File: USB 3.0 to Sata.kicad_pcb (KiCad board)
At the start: 4 copper layers, 27.8 x 45 mm, 35 parts, among them J1 USB_C_Receptacle, U3 VL716-Q4, U4 XUTS-2205-0429, U5 W25Q16BVSSIG, Y2 25Mhz Crystal

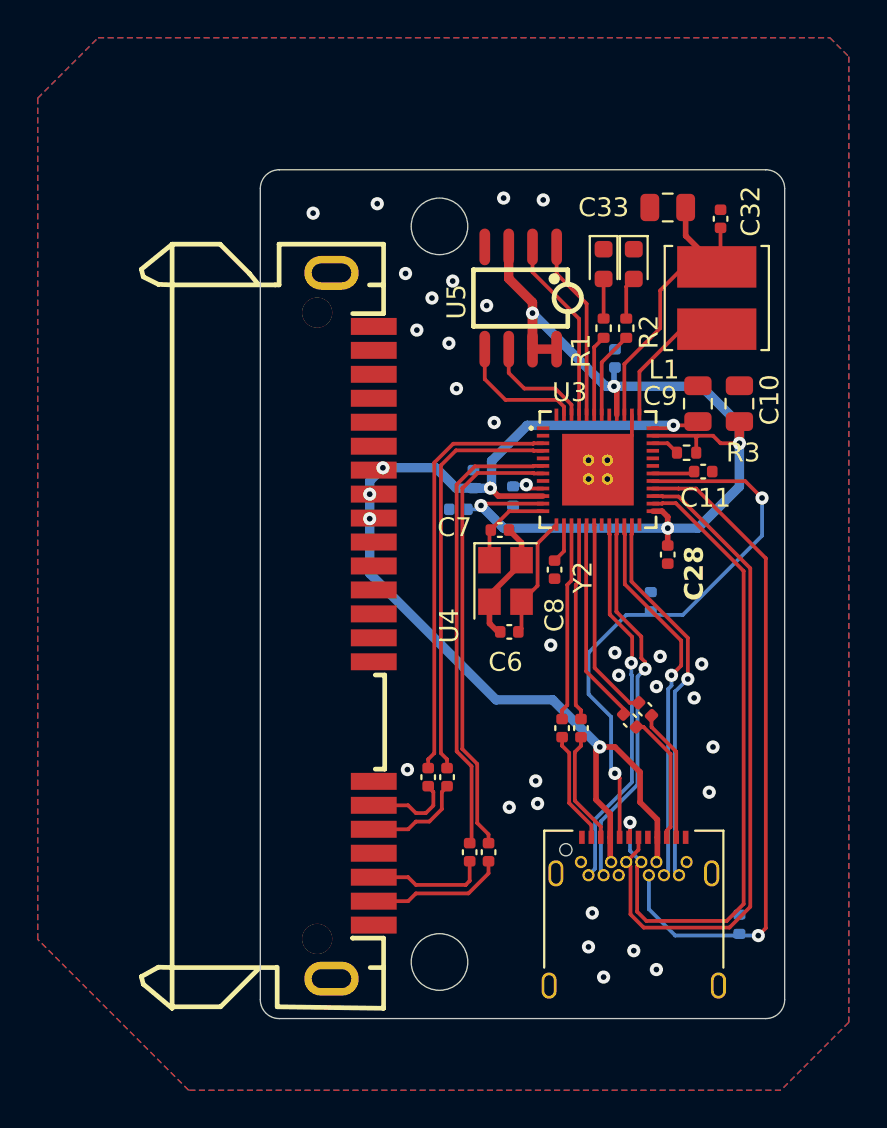
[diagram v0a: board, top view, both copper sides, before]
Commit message: Fixed pcb errors
Fixed RX2 TX2 lines being flipped, changed usb port footprint to the corect one, changed flash footprint from SOP8-150MIL to SOP8-208MIL
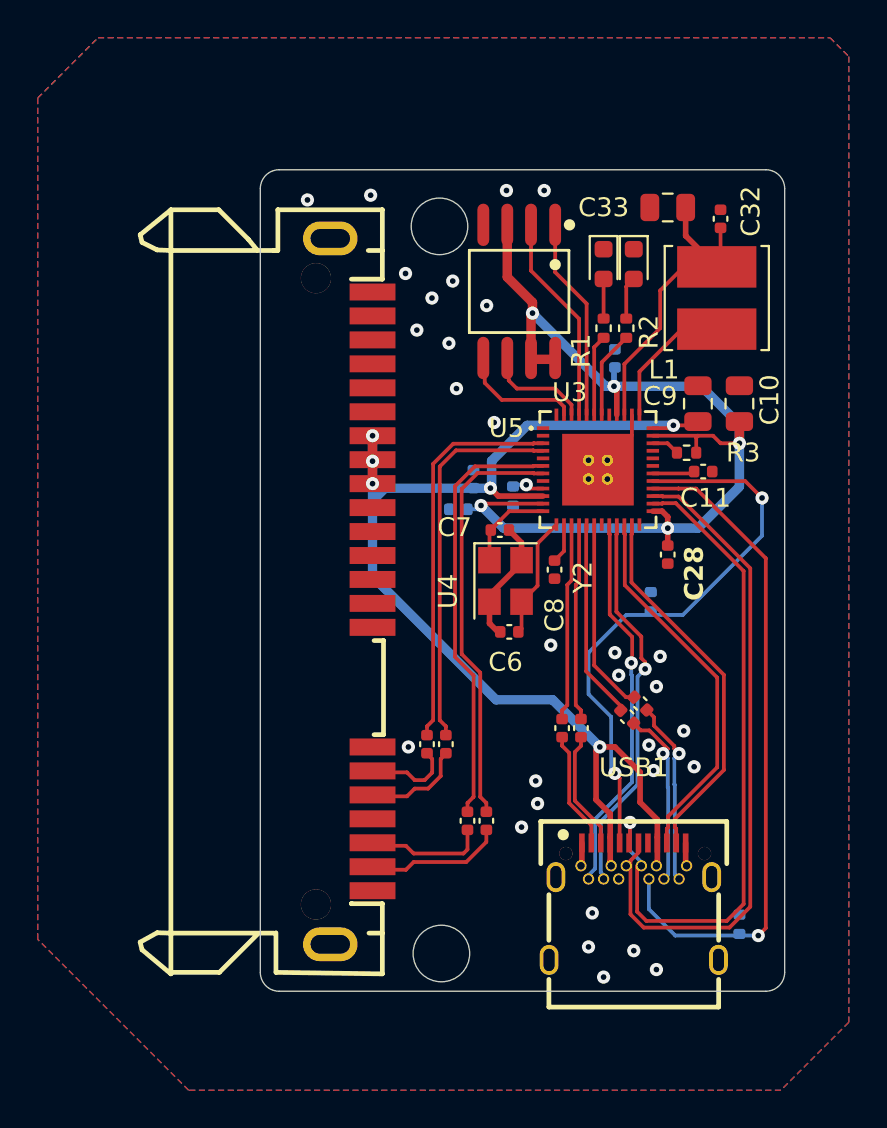
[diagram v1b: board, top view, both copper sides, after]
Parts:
- removed J1: USB_C_Receptacle, Connector_USB:USB_C_Receptacle_Amphenol_12401548E4-2A
- added USB1: TYPEC-324-BCP24, da:USB-C-SMD_TYPEC-324-BCP24, F.Cu at (59.8, 85.8)
- R4, R6: value 1K -> 5.1k
- U5: footprint da:SOIC-8_L5.0-W4.0-P1.27-LS6.0-BL -> da:SOIC-8_L5.3-W5.3-P1.27-LS8.0-BL
- moved U4 1.83 mm to (44.8, 69.3)
- moved C12 1.75 mm to (48.8, 77.5)
- moved C13 1.75 mm to (49.8, 77.5)
- moved C14 1.67 mm to (51.0, 81.5)
- moved C15 1.67 mm to (52.0, 81.5)
- moved C5 0.39 mm to (60.1, 75.3)
- moved U5 0.36 mm to (53.7, 53.5)
- moved C4 0.25 mm to (59.5, 76.0)
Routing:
- net VBUS: track 59.5 -> 64.1 mm
- net TX2+: track 6.99 -> 9.88 mm, vias 0 -> 1
- net TX2-: track 6.90 -> 9.58 mm, vias 0 -> 1
- net GND: track 7.80 -> 10.3 mm
- net SRXN: track 21.9 -> 20.2 mm
- net SRXP: track 22.5 -> 20.8 mm
- net STXP: track 24.0 -> 22.3 mm
- net STXN: track 24.4 -> 23.1 mm
- net SPI_DO: track 9.92 -> 11.1 mm
- net SPI_CS: track 9.56 -> 10.8 mm
- net /SATA_RXP: track 5.40 -> 4.64 mm
- net /SATA_RXN: track 6.15 -> 5.38 mm
- net RX2+: track 20.2 -> 20.0 mm, vias 1 -> 0
- net RX2-: track 20.2 -> 20.0 mm, vias 1 -> 0
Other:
- board size 27.8 x 45 mm -> 27.8 x 43.5 mm

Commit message: Fixed layout
Fixed traces length
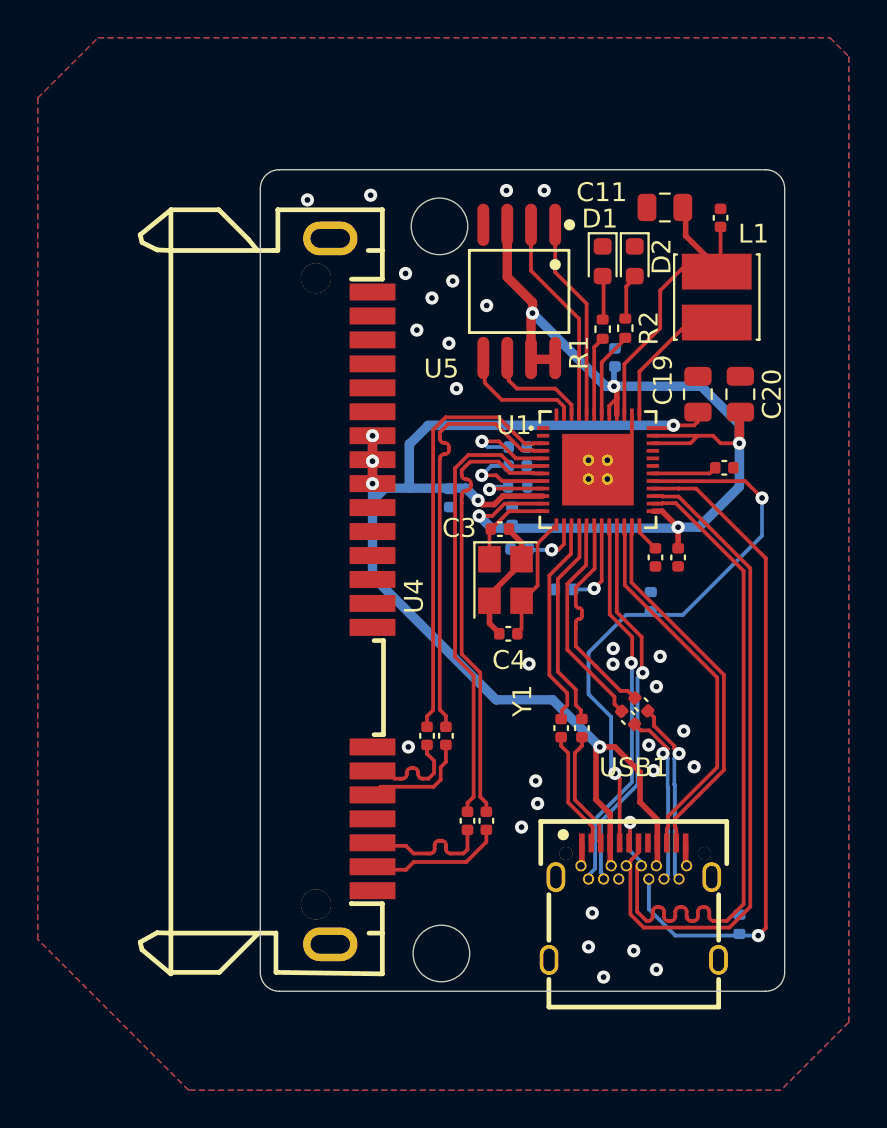
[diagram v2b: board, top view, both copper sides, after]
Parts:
- removed C28, C29, C30, C31, C32: 100nF, Capacitor_SMD:C_0402_1005Metric
- removed C33: 10uF, Capacitor_SMD:C_0805_2012Metric
- removed R5: 12.1K, Resistor_SMD:R_0402_1005Metric
- removed U3: VL716-Q4, da:QFN-48_L6.0-W6.0-P0.40-BL-EP3.8
- removed Y2: 25Mhz Crystal, Crystal:Crystal_SMD_3225-4Pin_3.2x2.5mm
- added C1: 100nF, Capacitor_SMD:C_0402_1005Metric, B.Cu at (53.4, 65.3)
- added C16: 100nF, Capacitor_SMD:C_0402_1005Metric, F.Cu at (64.4, 49.5)
- added C17: 100nF, Capacitor_SMD:C_0402_1005Metric, F.Cu at (64.6, 62.8)
- added C18: 100nF, Capacitor_SMD:C_0402_1005Metric, F.Cu at (62.1, 67.5)
- added C19: 10uF, Capacitor_SMD:C_0805_2012Metric, F.Cu at (63.2, 58.9)
- added C20: 10uF, Capacitor_SMD:C_0805_2012Metric, F.Cu at (65.5, 58.9)
- added C23: 100nF, Capacitor_SMD:C_0402_1005Metric, B.Cu at (53.6, 62.7)
- added C24: 100nF, Capacitor_SMD:C_0402_1005Metric, B.Cu at (53.6, 61.7)
- added C25: 100nF, Capacitor_SMD:C_0402_1005Metric, B.Cu at (56.1, 69.2)
- added C26: 100nF, Capacitor_SMD:C_0402_1005Metric, F.Cu at (61.0, 67.5)
- added U1: VL716-Q4, da:QFN-48_L6.0-W6.0-P0.40-BL-EP3.8, F.Cu at (57.9, 62.9)
- added Y1: 25Mhz Crystal, Crystal:Crystal_SMD_3225-4Pin_3.2x2.5mm, F.Cu at (53.0, 68.8)
- C10: value 10uF -> 100nF; footprint Capacitor_SMD:C_0805_2012Metric -> Capacitor_SMD:C_0402_1005Metric; moved to B.Cu
- C11: value 100nF -> 10uF; footprint Capacitor_SMD:C_0402_1005Metric -> Capacitor_SMD:C_0805_2012Metric
- C2, C5: moved to B.Cu
- C3, C4: value 100nF -> 20pF
- C6, C7: value 20pF -> 100nF
- C9: value 10uF -> 100nF; footprint Capacitor_SMD:C_0805_2012Metric -> Capacitor_SMD:C_0402_1005Metric
- L1: value ?uH -> 2.2uH; footprint Inductor_SMD:L_Cenker_CKCS5040 -> Inductor_SMD:L_Cenker_CKCS4030
- R3: value 10K -> 12.1K; moved to B.Cu
- moved C9 16.2 mm to (60.2, 75.3), turned to -45 degrees
- moved C11 14.1 mm to (61.5, 49.0), turned to 180 degrees
- moved C2 13.6 mm to (50.0, 64.4)
- moved C3 11.4 mm to (52.7, 66.0), turned to 0 degrees
- moved C7 11.4 mm to (57.0, 76.6), turned to -90 degrees
- moved C5 10.4 mm to (53.8, 67.1), turned to 0 degrees
- moved R3 9.13 mm to (53.6, 63.8)
- moved C8 8.76 mm to (59.5, 76.0), turned to -45 degrees
- moved C4 7.68 mm to (53.1, 71.6), turned to 0 degrees
- moved C10 7.04 mm to (58.8, 57.0), turned to 90 degrees
- moved C6 5.79 mm to (56.0, 76.6), turned to -90 degrees
- moved C12 0.44 mm to (48.8, 77.0)
- moved C13 0.44 mm to (49.8, 77.0)
- moved D1 0.16 mm to (58.1, 51.9)
- moved D2 0.16 mm to (59.9, 51.9)
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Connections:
- C10 pad 1: GND -> +3.3V
- C10 pad 2: +3.3V -> GND
- C11 pad 1: Net-(U3-VDD12I) -> Net-(U1-DCVCC12)
- C2 pad 1: /UTX1+ -> VBUS
- C2 pad 2: TX1+ -> GND
- C3 pad 1: /UTX1- -> Net-(U1-OSCXI)
- C3 pad 2: TX1- -> GND
- C4 pad 1: /UTX2- -> GND
- C4 pad 2: TX2- -> Net-(U1-OSCXO)
- C5 pad 1: /UTX2+ -> GND
- C5 pad 2: TX2+ -> Net-(U1-OSCVDD12)
- C6 pad 1: GND -> /VL716/UTX1+
- C6 pad 2: Net-(U3-OSCXO) -> TX1+
- C7 pad 1: Net-(U3-OSCXI) -> /VL716/UTX1-
- C7 pad 2: GND -> TX1-
- C8 pad 1: GND -> /VL716/UTX2-
- C8 pad 2: Net-(U3-OSCVDD12) -> TX2-
- C9 pad 1: GND -> /VL716/UTX2+
- C9 pad 2: VBUS -> TX2+
- L1 pad 1: Net-(U3-DCVCC12) -> Net-(U1-DCVCC12)
- R3 pad 1: +3.3V -> GND
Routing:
- net Net-(U3-DCVCC12): track 16.9 -> 0.00 mm
- net Net-(U1-DCVCC12): track 0.00 -> 16.9 mm
- net /VL716/UTX2-: track 0.00 -> 11.6 mm
- net /VL716/UTX2+: track 0.00 -> 11.5 mm
- net /VL716/UTX1-: track 0.00 -> 11.3 mm
- net /VL716/UTX1+: track 0.00 -> 11.3 mm
- net /UTX2-: track 10.6 -> 0.00 mm
- net /UTX1+: track 10.5 -> 0.00 mm
- net /UTX1-: track 10.5 -> 0.00 mm
- net /UTX2+: track 10.3 -> 0.00 mm
- net Net-(U3-OSCXO): track 6.53 -> 0.00 mm
- net Net-(U1-OSCXO): track 0.00 -> 6.53 mm
- net VBUS: track 64.1 -> 69.9 mm
- net SARXVDD12: track 0.00 -> 5.26 mm, vias 0 -> 1
- net SATXVDD12: track 0.00 -> 5.01 mm, vias 0 -> 1
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
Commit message: .
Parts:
- removed C23, C24: 100nF, Capacitor_SMD:C_0402_1005Metric
- added C21: 22uF, Capacitor_SMD:C_0805_2012Metric, F.Cu at (47.6, 60.1)
- added C22: 22uF, Capacitor_SMD:C_0805_2012Metric, F.Cu at (47.6, 64.7)
- added C29: 100nF, Capacitor_SMD:C_0402_1005Metric, B.Cu at (53.6, 61.9)
- added C30: 100nF, Capacitor_SMD:C_0402_1005Metric, B.Cu at (53.6, 62.9)
- moved C1 4.06 mm to (57.4, 65.4)
- moved C5 0.93 mm to (54.4, 67.8), turned to 90 degrees
- moved U4 0.78 mm to (44.1, 69.3)
- moved C2 0.67 mm to (50.5, 64.9)
- moved C26 0.32 mm to (61.0, 67.9)
- moved C18 0.31 mm to (62.1, 67.9)
- moved R3 0.18 mm to (53.6, 64.0)
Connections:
- C11 pad 1: Net-(U1-DCVCC12) -> U3TXVDD12
- C16 pad 1: Net-(U1-DCVCC12) -> U3TXVDD12
- C17 pad 1: Net-(U1-VDD12I) -> U3TXVDD12
- C25 pad 2: USB3TXVDD12 -> U3TXVDD12
- C26 pad 2: USB3RXVDD12 -> U3TXVDD12
- C5 pad 2: Net-(U1-OSCVDD12) -> U3TXVDD12
- L1 pad 1: Net-(U1-DCVCC12) -> U3TXVDD12
- U1 pad 14: Net-(U1-OSCVDD12) -> U3TXVDD12
- U1 pad 19: USB3TXVDD12 -> U3TXVDD12
- U1 pad 24: USB3RXVDD12 -> U3TXVDD12
- U1 pad 30: Net-(U1-VDD12I) -> U3TXVDD12
- U1 pad 39: Net-(U1-DCVCC12) -> U3TXVDD12
- U1 pad 5: SARXVDD12 -> U3TXVDD12
- U1 pad 8: SATXVDD12 -> U3TXVDD12
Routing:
- net U3TXVDD12: track 0.00 -> 79.8 mm, vias 0 -> 8
- net VBUS: track 69.9 -> 27.4 mm, vias 6 -> 7
- net Net-(U1-DCVCC12): track 16.9 -> 0.00 mm
- net SARXVDD12: track 5.26 -> 0.00 mm, vias 1 -> 0
- net SATXVDD12: track 5.01 -> 0.00 mm, vias 1 -> 0
- net USB3TXVDD12: track 4.70 -> 0.00 mm, vias 1 -> 0
- net Net-(U1-VDD12I): track 3.43 -> 0.00 mm
- net Net-(U1-OSCVDD12): track 3.05 -> 0.00 mm, vias 1 -> 0
- net USB3RXVDD12: track 1.61 -> 0.00 mm
- net +3.3V: track 59.2 -> 58.5 mm
- net /SATA_RXN: track 5.91 -> 6.55 mm
- net RX1+: track 20.1 -> 20.6 mm
- net GND: vias 29 -> 27
- added copper zone on B.Cu, net VBUS
- added copper zone on F.Cu, net VBUS
